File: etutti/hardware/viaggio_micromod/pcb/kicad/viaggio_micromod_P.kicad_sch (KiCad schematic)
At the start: 6 parts, among them J101 APCI0108-P001A

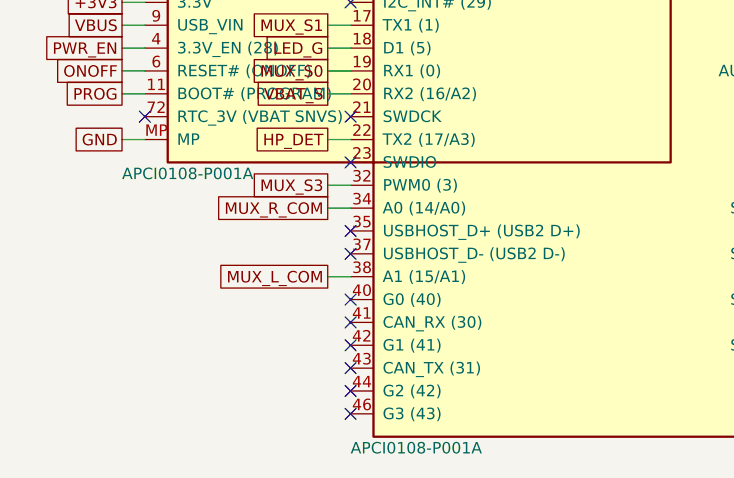
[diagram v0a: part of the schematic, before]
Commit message: eTutti Viaggio MicroMod SPEC v2.3 step M2: placed board for routing
- M2a: E2 (USBLC6) on top; J101 = UMAX 91302-42-067RCE (C48985906, 622 in
  stock at LCSC on 25 Oct 2026; LOTES C841659 out of stock), footprint from
  the UMAX drawing; H101 stays Wurth 9774025151R (Global Sourcing).
  ERC 0/0, netlist matches.
- M2b: build_board.py (no router, fails if any track appears) places every
  part from viaggio_micromod.json; outline, M2 holes, silkscreen; In1 = GND
  power plane, In2 = signal with no zones; vias 0.5/0.3 in every class;
  .kicad_dru compiles in KiCad 10 (units in mm, min 0.15 signals, Corrente
  >= 0.8 outside the power/connector courtyards, <= 1.9 mm under the card).
- Delivery DRC: 0 errors, 0 warnings, parity 0, 431 connections to route.
  DSN, top/bottom renders, ROTEAMENTO.md, ELETRONICA.md updated.
- Nothing routed, nothing ordered.

Co-Authored-By: Claude Opus 5.5 <noreply@anthropic.com>
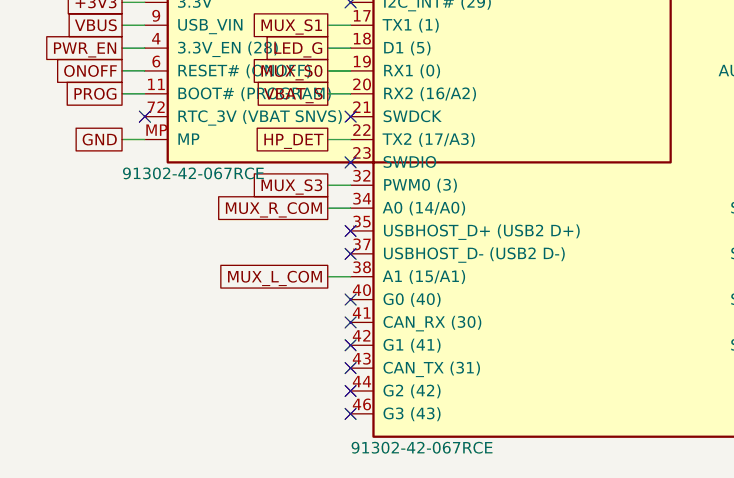
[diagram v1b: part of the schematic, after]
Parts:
- J101: value APCI0108-P001A -> 91302-42-067RCE; footprint viaggio_micromod:M.2_Socket_E_H4.2_MicroMod -> viaggio_micromod:M.2_E_H4.2_UMAX_91302-42-067; LCSC C841659 -> C48985906
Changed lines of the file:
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@@
 	(symbol (lib_id "viaggio_micromod:MicroMod_M.2_E") (at 58.42 66.04 0) (unit 1) (exclude_from_sim no) (in_bom yes) (on_board yes) (dnp no)
 		(property "Reference" "J101" (at 25.4 44.45 0) (effects (font (size 1.27 1.27)) (justify left)))
-		(property "Value" "APCI0108-P001A" (at 25.4 87.63 0) (effects (font (size 1.27 1.27)) (justify left)))
-		(property "Footprint" "viaggio_micromod:M.2_Socket_E_H4.2_MicroMod" (at 58.42 66.04 0) (hide yes) (effects (font (size 1.27 1.27))))
-		(property "Datasheet" "https://www.lcsc.com/datasheet/C841659.pdf" (at 58.42 66.04 0) (hide yes) (effects (font (size 1.27 1.27))))
-		(property "Description" "M.2 Key E 67 pinos, 0,5 mm, 4,2 mm (LOTES; equivalente ao TE 2199230-4 da SparkFun; conferir estoque e o desenho LOTES contra o footprint do TE); no verso; modulo SparkFun MicroMod Teensy DEV-16402 encaixado em casa" (at 58.42 66.04 0) (hide yes) (effects (font (size 1.27 1.27))))
+		(property "Value" "91302-42-067RCE" (at 25.4 87.63 0) (effects (font (size 1.27 1.27)) (justify left)))
+		(property "Footprint" "viaggio_micromod:M.2_E_H4.2_UMAX_91302-42-067" (at 58.42 66.04 0) (hide yes) (effects (font (size 1.27 1.27))))
+		(property "Datasheet" "https://datasheet.lcsc.com/datasheet/pdf/fa57621554b717c54a395d0658cff748.pdf?productCode=C48985906" (at 58.42 66.04 0) (hide yes) (effects (font (size 1.27 1.27))))
+		(property "Description" "UMAX M.2 Key E 67 pinos, 0,5 mm, 4,2 mm (estoque LCSC 622 em 25 out 2026; o LOTES C841659 estava com 0); footprint pelo desenho UMAX C-91302-42 rev C; no verso; modulo SparkFun MicroMod Teensy DEV-16402 encaixado em casa" (at 58.42 66.04 0) (hide yes) (effects (font (size 1.27 1.27))))
 		(property "Codigo" "P1" (at 30.48 44.45 0) (effects (font (size 1.27 1.27)) (justify right)))
-		(property "LCSC" "C841659" (at 58.42 66.04 0) (hide yes) (effects (font (size 1.27 1.27))))
+		(property "LCSC" "C48985906" (at 58.42 66.04 0) (hide yes) (effects (font (size 1.27 1.27))))
 		(property "Montagem" "JLC" (at 58.42 66.04 0) (hide yes) (effects (font (size 1.27 1.27))))
 		(pin "1")
@@
 	(symbol (lib_id "viaggio_micromod:MicroMod_M.2_E") (at 81.28 81.28 0) (unit 2) (exclude_from_sim no) (in_bom yes) (on_board yes) (dnp no)
 		(property "Reference" "J101" (at 50.8 44.45 0) (effects (font (size 1.27 1.27)) (justify left)))
-		(property "Value" "APCI0108-P001A" (at 50.8 118.11 0) (effects (font (size 1.27 1.27)) (justify left)))
-		(property "Footprint" "viaggio_micromod:M.2_Socket_E_H4.2_MicroMod" (at 81.28 81.28 0) (hide yes) (effects (font (size 1.27 1.27))))
-		(property "Datasheet" "https://www.lcsc.com/datasheet/C841659.pdf" (at 81.28 81.28 0) (hide yes) (effects (font (size 1.27 1.27))))
-		(property "Description" "M.2 Key E 67 pinos, 0,5 mm, 4,2 mm (LOTES; equivalente ao TE 2199230-4 da SparkFun; conferir estoque e o desenho LOTES contra o footprint do TE); no verso; modulo SparkFun MicroMod Teensy DEV-16402 encaixado em casa" (at 81.28 81.28 0) (hide yes) (effects (font (size 1.27 1.27))))
+		(property "Value" "91302-42-067RCE" (at 50.8 118.11 0) (effects (font (size 1.27 1.27)) (justify left)))
+		(property "Footprint" "viaggio_micromod:M.2_E_H4.2_UMAX_91302-42-067" (at 81.28 81.28 0) (hide yes) (effects (font (size 1.27 1.27))))
+		(property "Datasheet" "https://datasheet.lcsc.com/datasheet/pdf/fa57621554b717c54a395d0658cff748.pdf?productCode=C48985906" (at 81.28 81.28 0) (hide yes) (effects (font (size 1.27 1.27))))
+		(property "Description" "UMAX M.2 Key E 67 pinos, 0,5 mm, 4,2 mm (estoque LCSC 622 em 25 out 2026; o LOTES C841659 estava com 0); footprint pelo desenho UMAX C-91302-42 rev C; no verso; modulo SparkFun MicroMod Teensy DEV-16402 encaixado em casa" (at 81.28 81.28 0) (hide yes) (effects (font (size 1.27 1.27))))
 		(property "Codigo" "P1" (at 111.76 44.45 0) (effects (font (size 1.27 1.27)) (justify right)))
-		(property "LCSC" "C841659" (at 81.28 81.28 0) (hide yes) (effects (font (size 1.27 1.27))))
+		(property "LCSC" "C48985906" (at 81.28 81.28 0) (hide yes) (effects (font (size 1.27 1.27))))
 		(property "Montagem" "JLC" (at 81.28 81.28 0) (hide yes) (effects (font (size 1.27 1.27))))
 		(pin "3")
@@
 		(property "Footprint" "viaggio_micromod:Standoff_SMD_M2.5_H2.5" (at 137.16 45.72 0) (hide yes) (effects (font (size 1.27 1.27))))
 		(property "Datasheet" "https://www.we-online.com/components/products/datasheet/9774025151R.pdf" (at 137.16 45.72 0) (hide yes) (effects (font (size 1.27 1.27))))
-		(property "Description" "espacador SMD M2.5 x 2,5 mm (Wurth WA-SMSI, o da SparkFun); a (+4,0; -20,0) do J101 nas coordenadas do footprint; sem codigo LCSC confirmado (alternativa a medir: YIYUAN SMTSOM2.520BTR C5301776, 2,0 mm); parafuso M2.5 x 3 cabeca chata em casa" (at 137.16 45.72 0) (hide yes) (effects (font (size 1.27 1.27))))
+		(property "Description" "espacador SMD M2.5 x 2,5 mm (Wurth WA-SMSI, o da SparkFun; SPEC v2.3); a (+4,0; -20,0) do J101 nas coordenadas do footprint; sem equivalente LCSC de 2,5 mm com estoque em 25 out 2026 (YIYUAN SMTSOM2.520BTR C5301776: 2,0 mm, estoque 0); parafuso M2.5 x 3 cabeca chata em casa" (at 137.16 45.72 0) (hide yes) (effects (font (size 1.27 1.27))))
 		(property "Codigo" "P1" (at 139.7 44.45 0) (effects (font (size 1.27 1.27)) (justify right)))
 		(property "LCSC" "" (at 137.16 45.72 0) (hide yes) (effects (font (size 1.27 1.27))))
